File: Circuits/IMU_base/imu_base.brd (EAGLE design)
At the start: 16.7 x 12.1 mm, 11 parts, among them U1 LSM9DS1

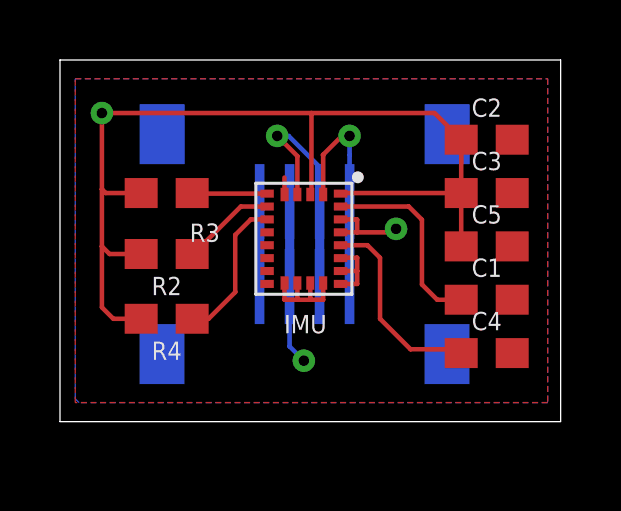
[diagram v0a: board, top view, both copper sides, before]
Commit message: connected 6 conn package and symbol, base board layout complete
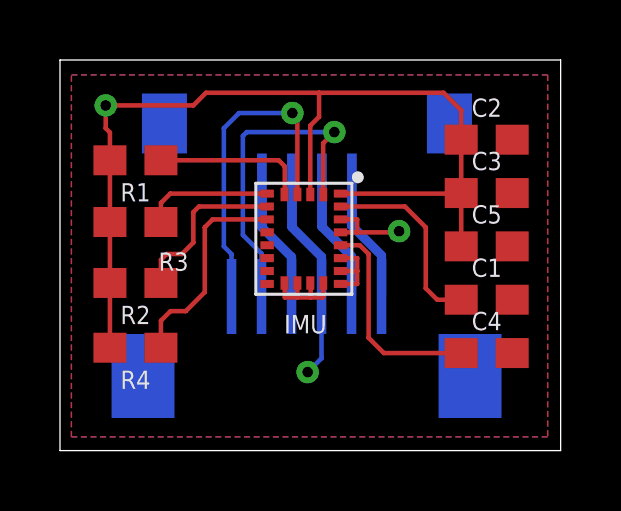
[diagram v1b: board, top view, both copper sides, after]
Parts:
- added R1: 10k, SparkFun-Resistors:0603
- U$2: value MOLEX_522070433 -> MOLEX_522070633; device custom:MOLEX4_1MM -> custom:MOLEX6_1MM
- moved U$2 6.89 mm to (50.1, 31.9), turned to 0 degrees
- moved U$1 6.31 mm to (46.1, 37.8), turned to 180 degrees
- moved R3 1.42 mm to (41.9, 35.6)
- moved R4 1.42 mm to (41.9, 31.4)
- moved R2 1.42 mm to (41.9, 33.6)
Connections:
- new net SA0: R1.1, U1.5
- new net SCL1: U$2.5, U1.2
- new net SDA1: U$2.6, U1.4
- net GND: now also U$1.2, U$2.3; no longer U$1.3, U$2.2, U1.5
- net SCL: now also U$1.4, U$2.1; no longer U$1.1, U$2.4, U1.2
- net SDA: now also U$1.3, U$2.2; no longer U$1.2, U$2.3, U1.4
- net VCC: now also R1.2, U$1.1, U$2.4; no longer U$1.4, U$2.1
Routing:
- net SDA1: track 0.00 -> 11.0 mm, vias 0 -> 1
- net SCL1: track 0.00 -> 10.9 mm, vias 0 -> 1
- net SA0: track 0.00 -> 5.15 mm
- net SDA: track 8.07 -> 3.93 mm, vias 1 -> 0
- net SCL: track 7.50 -> 3.93 mm, vias 1 -> 0
- net CS_A/G: track 3.15 -> 5.64 mm
- net CS_M: track 4.98 -> 7.10 mm
- net SA1: track 2.50 -> 4.30 mm
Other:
- board size 16.7 x 12.1 mm -> 16.7 x 13 mm

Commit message: Added testpad in schematic and board layout to allow address to be pulled up or down when needed
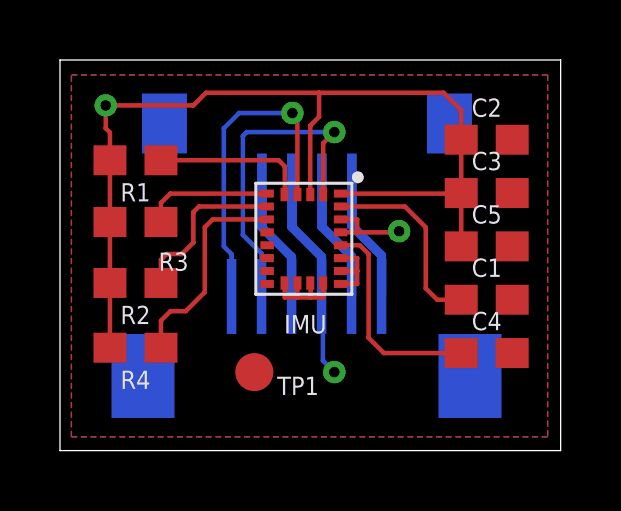
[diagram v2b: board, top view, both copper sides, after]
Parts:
- added TP1: TPB1,27, testpad:B1,27
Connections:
- net GND: now also TP1.TP
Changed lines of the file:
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@@
 <drawing>
 <settings>
-<setting alwaysvectorfont="no"/>
+<setting alwaysvectorfont="yes"/>
 <setting verticaltext="up"/>
 </settings>
@@
 <layer number="24" name="bOrigins" color="15" fill="1" visible="yes" active="yes"/>
 <layer number="25" name="tNames" color="7" fill="1" visible="yes" active="yes"/>
-<layer number="26" name="bNames" color="7" fill="1" visible="no" active="yes"/>
+<layer number="26" name="bNames" color="7" fill="1" visible="yes" active="yes"/>
 <layer number="27" name="tValues" color="7" fill="1" visible="no" active="yes"/>
 <layer number="28" name="bValues" color="7" fill="1" visible="no" active="yes"/>
@@
 <attribute name="VALUE" x="50.9388" y="26.8278" size="1.27" layer="28" rot="MR0"/>
 </element>
+<element name="TP1" library="testpad" library_urn="urn:adsk.eagle:library:385" package="B1,27" package3d_urn="urn:adsk.eagle:package:27944/2" value="TPB1,27" x="45.847" y="30.607" smashed="yes">
+<attribute name="NAME" x="46.609" y="29.845" size="0.6096" layer="25" ratio="10"/>
+<attribute name="TP_SIGNAL_NAME" value="" x="45.847" y="30.607" size="1.778" layer="27" display="off"/>
+<attribute name="VALUE" x="45.212" y="29.845" size="0.0254" layer="27"/>
+</element>
 </elements>
 <signals>
@@
 <wire x1="48.0888" y1="34.44961875" x2="48.0888" y2="33.1278" width="0.3048" layer="16"/>
 <wire x1="47.101" y1="35.437421875" x2="48.0888" y2="34.44961875" width="0.3048" layer="16"/>
-<via x="47.625" y="30.607" extent="1-16" drill="0.35"/>
-<wire x1="47.625" y1="30.607" x2="48.0888" y2="31.0708" width="0.1524" layer="16"/>
-<wire x1="48.0888" y1="31.0708" x2="48.0888" y2="33.1278" width="0.1524" layer="16"/>
+<via x="48.514" y="30.607" extent="1-16" drill="0.35"/>
 <polygon width="0.1524" layer="1">
 <vertex x="39.751" y="40.513"/>
@@
 <vertex x="39.751" y="28.448"/>
 </polygon>
+<wire x1="48.0888" y1="33.1278" x2="48.133" y2="33.0836" width="0.1524" layer="16"/>
+<wire x1="48.133" y1="33.0836" x2="48.133" y2="30.988" width="0.1524" layer="16"/>
+<wire x1="48.133" y1="30.988" x2="48.514" y2="30.607" width="0.1524" layer="16"/>
+<contactref element="TP1" pad="TP"/>
 </signal>
 <signal name="C1">
@@
 </board>
 </drawing>
+<compatibility>
+<note version="8.2" severity="warning">
+Since Version 8.2, EAGLE supports online libraries. The ids
+of those online libraries will not be understood (or retained)
+with this version.
+</note>
+<note version="8.3" severity="warning">
+Since Version 8.3, EAGLE supports URNs for individual library
+assets (packages, symbols, and devices). The URNs of those assets
+will not be understood (or retained) with this version.
+</note>
+<note version="8.3" severity="warning">
+Since Version 8.3, EAGLE supports the association of 3D packages
+with devices in libraries, schematics, and board files. Those 3D
+packages will not be understood (or retained) with this version.
+</note>
+</compatibility>
 </eagle>

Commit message: change test pad size up
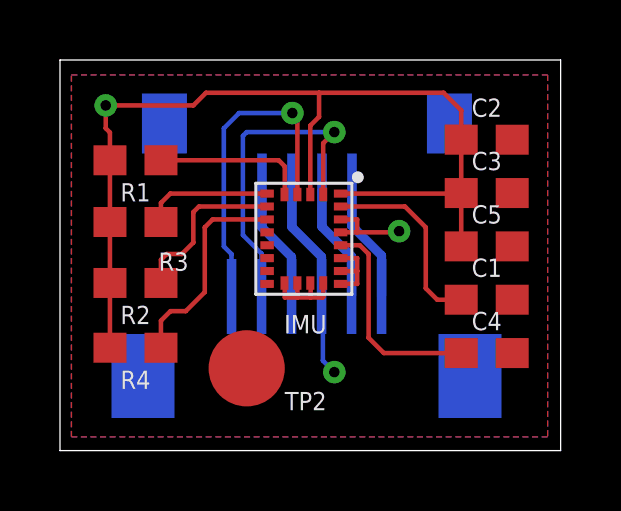
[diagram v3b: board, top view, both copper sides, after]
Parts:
- removed TP1: TPB1,27, testpad:B1,27
- added TP2: TPB2,54, testpad:B2,54
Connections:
- net GND: now also TP2.TP; no longer TP1.TP
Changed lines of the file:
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@@
 <drawing>
 <settings>
-<setting alwaysvectorfont="yes"/>
+<setting alwaysvectorfont="no"/>
 <setting verticaltext="up"/>
 </settings>
@@
 <attribute name="VALUE" x="50.9388" y="26.8278" size="1.27" layer="28" rot="MR0"/>
 </element>
-<element name="TP1" library="testpad" library_urn="urn:adsk.eagle:library:385" package="B1,27" package3d_urn="urn:adsk.eagle:package:27944/2" value="TPB1,27" x="45.847" y="30.607" smashed="yes">
-<attribute name="NAME" x="46.609" y="29.845" size="0.6096" layer="25" ratio="10"/>
-<attribute name="TP_SIGNAL_NAME" value="" x="45.847" y="30.607" size="1.778" layer="27" display="off"/>
-<attribute name="VALUE" x="45.212" y="29.845" size="0.0254" layer="27"/>
+<element name="TP2" library="testpad" library_urn="urn:adsk.eagle:library:385" package="B2,54" package3d_urn="urn:adsk.eagle:package:27948/1" value="TPB2,54" x="45.593" y="30.734" smashed="yes">
+<attribute name="NAME" x="46.863" y="29.337" size="0.6096" layer="25" ratio="10"/>
+<attribute name="TP_SIGNAL_NAME" value="" x="45.593" y="30.734" size="1.778" layer="27" display="off"/>
+<attribute name="VALUE" x="44.323" y="29.337" size="0.0254" layer="27"/>
 </element>
 </elements>
@@
 <wire x1="48.133" y1="33.0836" x2="48.133" y2="30.988" width="0.1524" layer="16"/>
 <wire x1="48.133" y1="30.988" x2="48.514" y2="30.607" width="0.1524" layer="16"/>
-<contactref element="TP1" pad="TP"/>
+<contactref element="TP2" pad="TP"/>
 </signal>
 <signal name="C1">
